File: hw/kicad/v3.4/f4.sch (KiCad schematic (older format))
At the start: 44 parts

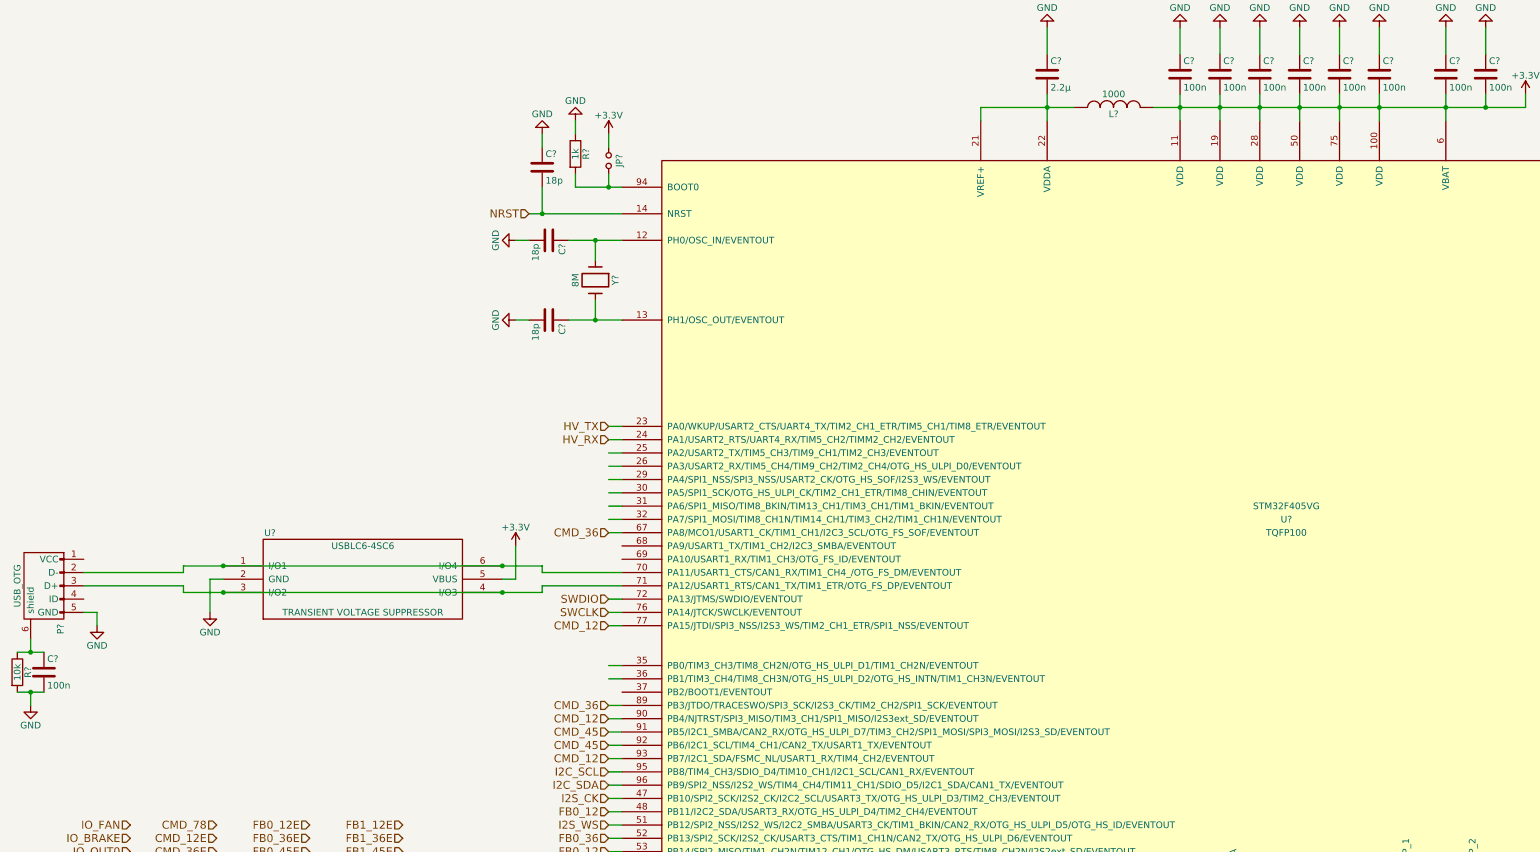
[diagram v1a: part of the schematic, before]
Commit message: f4 usb fix
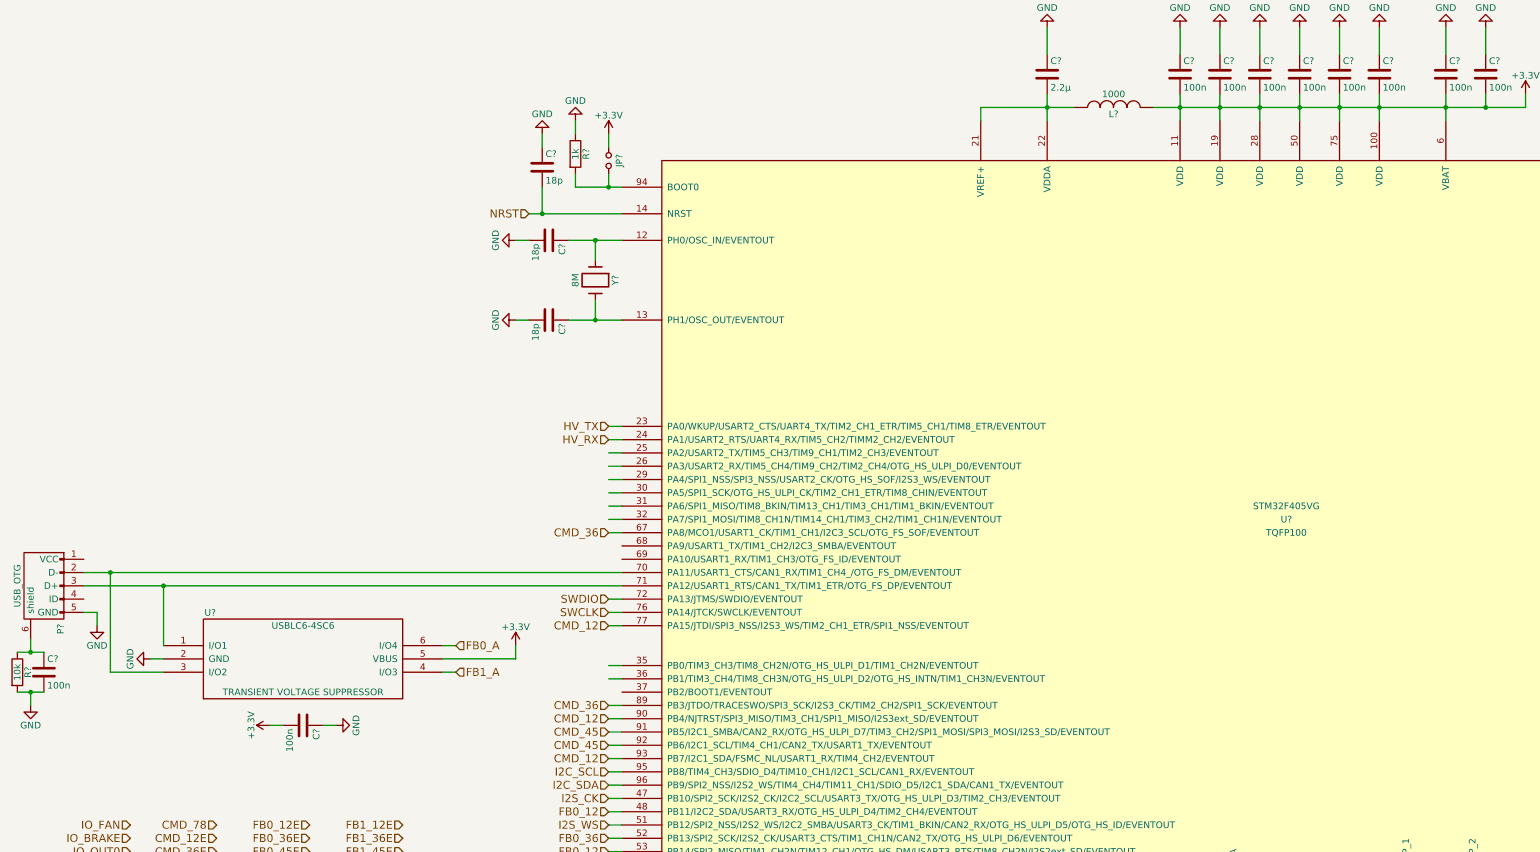
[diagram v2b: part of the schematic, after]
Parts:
- added C?: 100n, symbol C
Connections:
- wire segments 161 -> 159
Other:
- moved on the sheet: U?
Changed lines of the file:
@@
 	4800 3400 5200 3400
 Wire Wire Line
-	5200 4000 4800 4000
+	4800 4000 5200 4000
 Wire Wire Line
 	5000 3850 5000 4000
@@
 	9800 8500 9800 8600
 Wire Wire Line
-	11400 2500 11400 2300
-Wire Wire Line
-	10900 2500 10900 2300
-Wire Wire Line
-	10600 2500 10600 2300
-Wire Wire Line
-	10300 2500 10300 2300
-Wire Wire Line
-	10000 2500 10000 2300
-Wire Wire Line
-	9700 2500 9700 2300
-Wire Wire Line
-	9400 2500 9400 2300
+	11400 2300 11400 2500
+Wire Wire Line
+	10900 2300 10900 2500
+Wire Wire Line
+	10600 2300 10600 2500
+Wire Wire Line
+	10300 2300 10300 2500
+Wire Wire Line
+	10000 2300 10000 2500
+Wire Wire Line
+	9700 2300 9700 2500
+Wire Wire Line
+	9400 2300 9400 2500
 Wire Wire Line
 	9200 2400 12000 2400
@@
 	9400 2000 9400 1800
 Wire Wire Line
-	8400 2500 8400 2300
+	8400 2300 8400 2500
 $Comp
 L GND #PWR?
@@
 Text HLabel 1500 8100 0    60   Input ~ 0
 IO_OUT1
-Wire Wire Line
-	1900 5850 4600 5850
-Wire Wire Line
-	4600 5850 4600 5900
-Wire Wire Line
-	4600 5900 5200 5900
-Wire Wire Line
-	5200 6000 4600 6000
-Wire Wire Line
-	4600 6000 4600 6050
-Wire Wire Line
-	4600 6050 1900 6050
-Wire Wire Line
-	1900 6050 1900 6000
-Wire Wire Line
-	1900 6000 1150 6000
-Wire Wire Line
-	1150 5900 1900 5900
-Wire Wire Line
-	1900 5900 1900 5850
 $Comp
 L GND #PWR?
 U 1 1 5667D307
-P 2100 6200
-F 0 "#PWR?" H 2100 5950 50  0001 C CNN
-F 1 "GND" H 2100 6050 50  0000 C CNN
-F 2 "" H 2100 6200 60  0000 C CNN
-F 3 "" H 2100 6200 60  0000 C CNN
-	1    2100 6200
-	1    0    0    -1
-$EndComp
-Wire Wire Line
-	2100 6200 2100 5950
-Wire Wire Line
-	2100 5950 2200 5950
+P 1650 6550
+F 0 "#PWR?" H 1650 6300 50  0001 C CNN
+F 1 "GND" H 1650 6400 50  0000 C CNN
+F 2 "" H 1650 6550 60  0000 C CNN
+F 3 "" H 1650 6550 60  0000 C CNN
+	1    1650 6550
+	0    1    1    0
+$EndComp
 $Comp
 L +3.3V #PWR?
 U 1 1 5667D40D
-P 4400 5700
-F 0 "#PWR?" H 4400 5550 50  0001 C CNN
-F 1 "+3.3V" H 4400 5840 50  0000 C CNN
-F 2 "" H 4400 5700 60  0000 C CNN
-F 3 "" H 4400 5700 60  0000 C CNN
-	1    4400 5700
-	1    0    0    -1
-$EndComp
-Wire Wire Line
-	4400 5700 4400 5950
-Wire Wire Line
-	4400 5950 4300 5950
+P 4400 6450
+F 0 "#PWR?" H 4400 6300 50  0001 C CNN
+F 1 "+3.3V" H 4400 6590 50  0000 C CNN
+F 2 "" H 4400 6450 60  0000 C CNN
+F 3 "" H 4400 6450 60  0000 C CNN
+	1    4400 6450
+	1    0    0    -1
+$EndComp
 $Comp
 L USBLC6-4SC6 U?
 U 1 1 5667D8FF
-P 3250 5950
-F 0 "U?" H 2551 6298 50  0000 C CNN
-F 1 "USBLC6-4SC6" H 3250 6200 50  0000 C CNN
-F 2 "" H 3250 5950 60  0000 C CNN
-F 3 "" H 3250 5950 60  0000 C CNN
-F 4 "TRANSIENT VOLTAGE SUPPRESSOR" H 3250 5700 50  0000 C CNN "Description"
-	1    3250 5950
-	1    0    0    -1
-$EndComp
-Connection ~ 4300 6050
-Connection ~ 2200 6050
-Connection ~ 4300 5850
-Connection ~ 2200 5850
+P 2800 6550
+F 0 "U?" H 2101 6898 50  0000 C CNN
+F 1 "USBLC6-4SC6" H 2800 6800 50  0000 C CNN
+F 2 "" H 2800 6550 60  0000 C CNN
+F 3 "" H 2800 6550 60  0000 C CNN
+F 4 "TRANSIENT VOLTAGE SUPPRESSOR" H 2800 6300 50  0000 C CNN "Description"
+	1    2800 6550
+	1    0    0    -1
+$EndComp
 $Comp
 L USBLC6-4SC6 U?
@@
 Wire Wire Line
 	5100 2600 5100 2700
+Wire Wire Line
+	1150 6000 5200 6000
+Wire Wire Line
+	1150 5900 5200 5900
+Wire Wire Line
+	1750 6450 1750 6000
+Connection ~ 1750 6000
+Wire Wire Line
+	1750 6650 1350 6650
+Wire Wire Line
+	1350 6650 1350 5900
+Connection ~ 1350 5900
+Wire Wire Line
+	1650 6550 1750 6550
+Wire Wire Line
+	3850 6550 4400 6550
+Text HLabel 3950 6450 2    60   Input ~ 0
+FB0_A
+Text HLabel 3950 6650 2    60   Input ~ 0
+FB1_A
+Wire Wire Line
+	3850 6650 3950 6650
+Wire Wire Line
+	3850 6450 3950 6450
+$Comp
+L GND #PWR?
+U 1 1 56667EDB
+P 3050 7050
+F 0 "#PWR?" H 3050 6800 50  0001 C CNN
+F 1 "GND" H 3050 6900 50  0000 C CNN
+F 2 "" H 3050 7050 60  0000 C CNN
+F 3 "" H 3050 7050 60  0000 C CNN
+	1    3050 7050
+	0    -1   1    0
+$EndComp
+$Comp
+L +3.3V #PWR?
+U 1 1 566680A9
+P 2550 7050
+F 0 "#PWR?" H 2550 6900 50  0001 C CNN
+F 1 "+3.3V" H 2550 7190 50  0000 C CNN
+F 2 "" H 2550 7050 60  0000 C CNN
+F 3 "" H 2550 7050 60  0000 C CNN
+	1    2550 7050
+	0    -1   1    0
+$EndComp
+Wire Wire Line
+	3050 7050 2950 7050
+Wire Wire Line
+	2650 7050 2550 7050
+$Comp
+L C C?
+U 1 1 5666869C
+P 2800 7050
+F 0 "C?" H 2825 7150 50  0000 L CNN
+F 1 "100n" H 2825 6950 50  0000 L CNN
+F 2 "" H 2838 6900 30  0000 C CNN
+F 3 "" H 2800 7050 60  0000 C CNN
+	1    2800 7050
+	0    1    1    0
+$EndComp
+Wire Wire Line
+	4400 6550 4400 6450
 $EndSCHEMATC

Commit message: fb fix, cleanup
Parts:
- removed U? (x2): USBLC6-4SC6, symbol USBLC6-4SC6
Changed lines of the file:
@@
-	1    0    0    -1
-$EndComp
-$Comp
-L USBLC6-4SC6 U?
-U 1 1 5667DBA8
-P 5950 10500
-F 0 "U?" H 5251 10848 50  0000 C CNN
-F 1 "USBLC6-4SC6" H 5950 10750 50  0000 C CNN
-F 2 "" H 5950 10500 60  0000 C CNN
-F 3 "" H 5950 10500 60  0000 C CNN
-F 4 "TRANSIENT VOLTAGE SUPPRESSOR" H 5950 10250 50  0000 C CNN "Description"
-	1    5950 10500
-	1    0    0    -1
-$EndComp
-$Comp
-L USBLC6-4SC6 U?
-U 1 1 5667DC15
-P 8450 10500
-F 0 "U?" H 7751 10848 50  0000 C CNN
-F 1 "USBLC6-4SC6" H 8450 10750 50  0000 C CNN
-F 2 "" H 8450 10500 60  0000 C CNN
-F 3 "" H 8450 10500 60  0000 C CNN
-F 4 "TRANSIENT VOLTAGE SUPPRESSOR" H 8450 10250 50  0000 C CNN "Description"
-	1    8450 10500
 	1    0    0    -1
 $EndComp

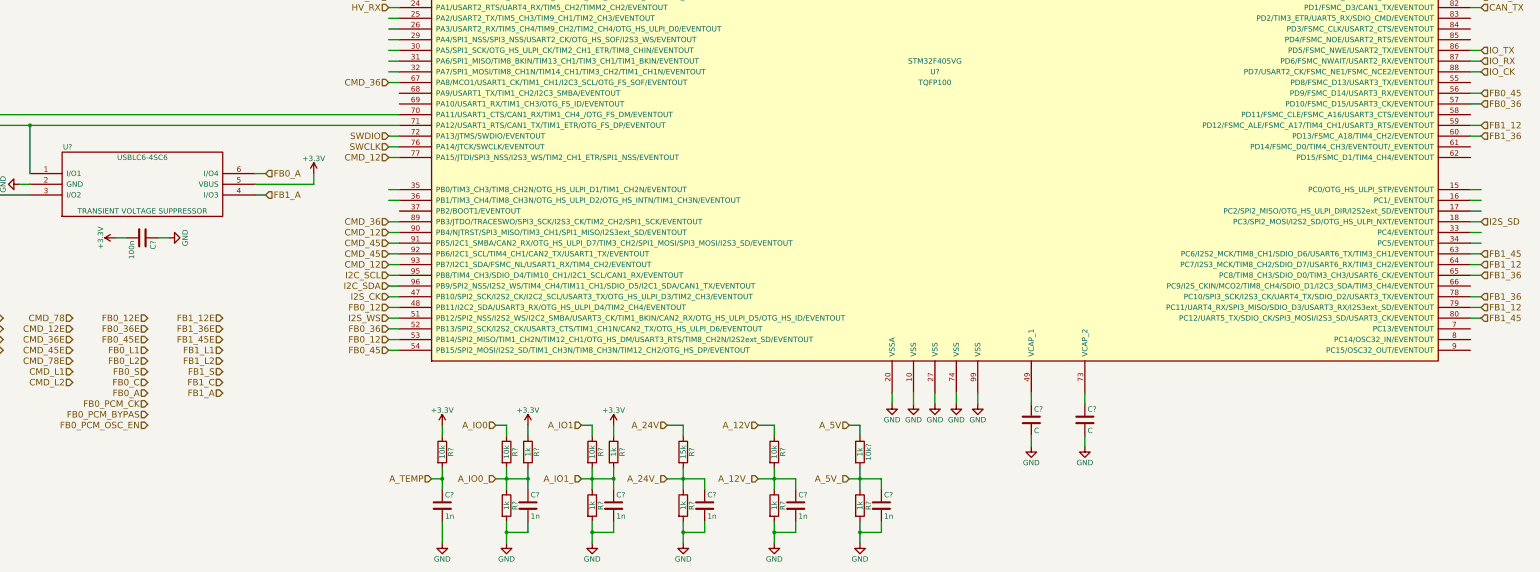
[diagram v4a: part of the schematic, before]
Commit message: +cur sense, f4 pin remap
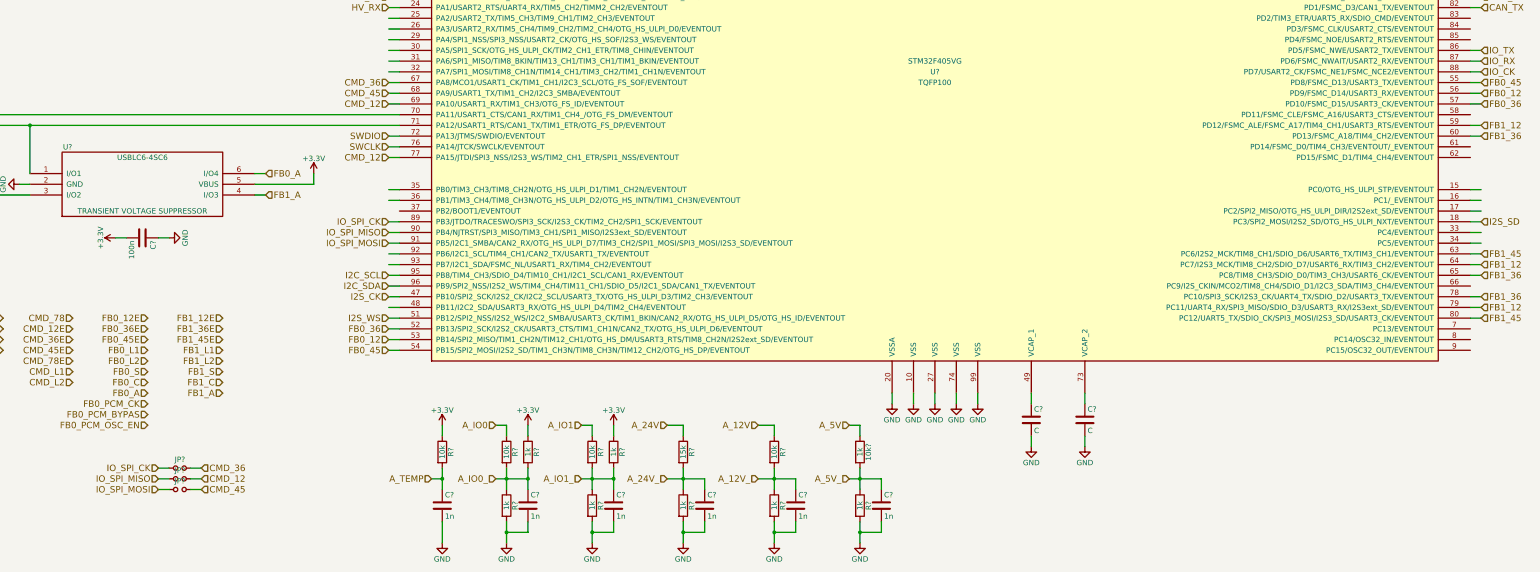
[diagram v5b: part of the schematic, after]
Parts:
- added JP? (x3): Jumper_NO_Small, symbol Jumper_NO_Small
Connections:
- net labels added: IO_SPI_CK, IO_SPI_MISO, IO_SPI_MOSI
- wire segments 159 -> 168
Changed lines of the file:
@@
 $Descr A3 16535 11693
 encoding utf-8
-Sheet 13 15
+Sheet 14 15
 Title ""
 Date ""
@@
 CMD_12
 Text HLabel 5100 7000 0    60   Input ~ 0
-CMD_12
-Text HLabel 5100 7300 0    60   Input ~ 0
+IO_SPI_MISO
+Text HLabel 5100 5800 0    60   Input ~ 0
 CMD_12
 Text HLabel 5100 5600 0    60   Input ~ 0
 CMD_36
 Text HLabel 5100 6900 0    60   Input ~ 0
-CMD_36
+IO_SPI_CK
 Text HLabel 5100 7100 0    60   Input ~ 0
-CMD_45
-Text HLabel 5100 7200 0    60   Input ~ 0
+IO_SPI_MOSI
+Text HLabel 5100 5700 0    60   Input ~ 0
 CMD_45
 Text HLabel 5100 8000 0    60   Input ~ 0
 FB0_12
-Text HLabel 5100 7700 0    60   Input ~ 0
+Text HLabel 15300 5700 2    60   Input ~ 0
 FB0_12
 Text HLabel 15300 3900 2    60   Input ~ 0
@@
 Text HLabel 15300 4100 2    60   Input ~ 0
 FB0_36
-Text HLabel 15300 5700 2    60   Input ~ 0
+Text HLabel 15300 5600 2    60   Input ~ 0
 FB0_45
 Text HLabel 5100 8100 0    60   Input ~ 0
@@
 Wire Wire Line
 	4400 6550 4400 6450
+Wire Wire Line
+	15300 5600 15200 5600
+Wire Wire Line
+	5100 5700 5200 5700
+Wire Wire Line
+	5100 5800 5200 5800
+$Comp
+L Jumper_NO_Small JP?
+U 1 1 5669DF96
+P 3150 9200
+F 0 "JP?" H 3150 9280 50  0000 C CNN
+F 1 "Jumper_NO_Small" H 3160 9140 50  0001 C CNN
+F 2 "" H 3150 9200 60  0000 C CNN
+F 3 "" H 3150 9200 60  0000 C CNN
+	1    3150 9200
+	1    0    0    -1
+$EndComp
+$Comp
+L Jumper_NO_Small JP?
+U 1 1 5669E03D
+P 3150 9300
+F 0 "JP?" H 3150 9380 50  0000 C CNN
+F 1 "Jumper_NO_Small" H 3160 9240 50  0001 C CNN
+F 2 "" H 3150 9300 60  0000 C CNN
+F 3 "" H 3150 9300 60  0000 C CNN
+	1    3150 9300
+	1    0    0    -1
+$EndComp
+$Comp
+L Jumper_NO_Small JP?
+U 1 1 5669E0D4
+P 3150 9400
+F 0 "JP?" H 3150 9480 50  0000 C CNN
+F 1 "Jumper_NO_Small" H 3160 9340 50  0001 C CNN
+F 2 "" H 3150 9400 60  0000 C CNN
+F 3 "" H 3150 9400 60  0000 C CNN
+	1    3150 9400
+	1    0    0    -1
+$EndComp
+Text HLabel 2950 9200 0    60   Input ~ 0
+IO_SPI_CK
+Text HLabel 2950 9300 0    60   Input ~ 0
+IO_SPI_MISO
+Text HLabel 2950 9400 0    60   Input ~ 0
+IO_SPI_MOSI
+Text HLabel 3350 9200 2    60   Input ~ 0
+CMD_36
+Text HLabel 3350 9400 2    60   Input ~ 0
+CMD_45
+Text HLabel 3350 9300 2    60   Input ~ 0
+CMD_12
+Wire Wire Line
+	2950 9200 3050 9200
+Wire Wire Line
+	2950 9300 3050 9300
+Wire Wire Line
+	2950 9400 3050 9400
+Wire Wire Line
+	3250 9200 3350 9200
+Wire Wire Line
+	3250 9300 3350 9300
+Wire Wire Line
+	3250 9400 3350 9400
 $EndSCHEMATC

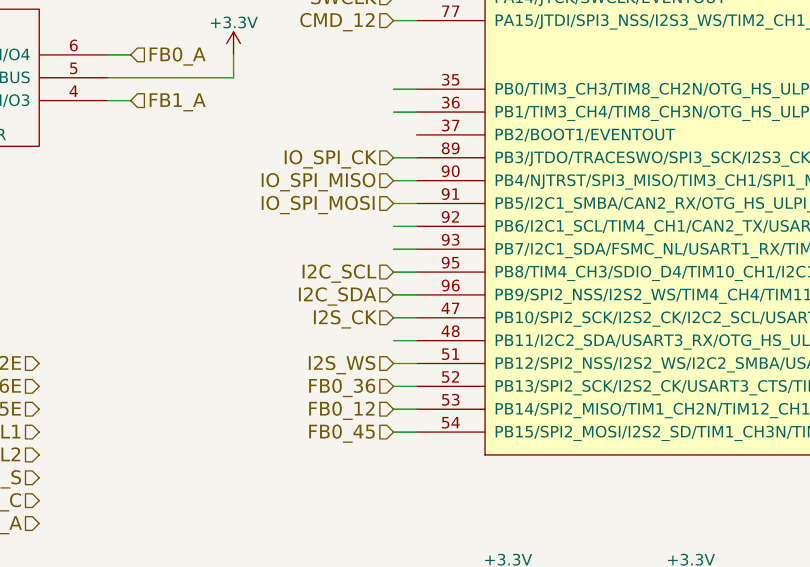
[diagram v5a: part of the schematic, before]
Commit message: io +spi
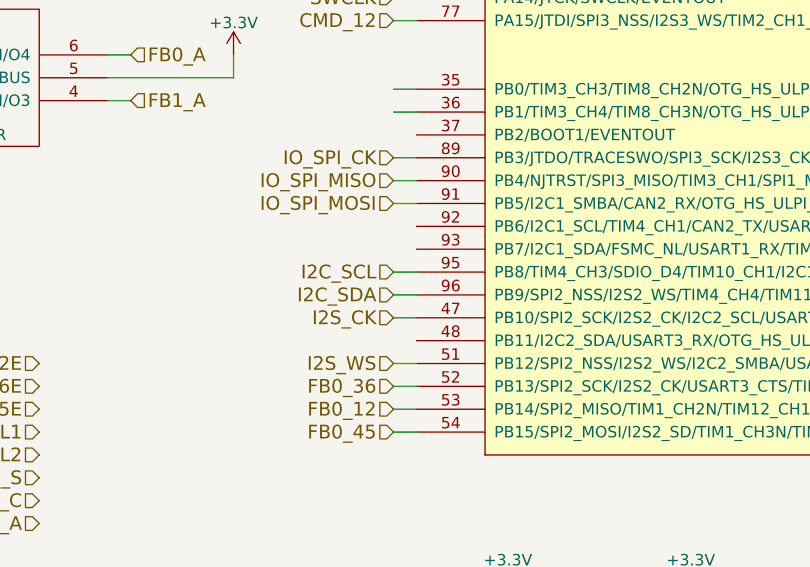
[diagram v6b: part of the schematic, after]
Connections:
- wire segments 168 -> 165
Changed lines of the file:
@@
 	5100 7000 5200 7000
-Wire Wire Line
-	5100 7300 5200 7300
 Wire Wire Line
 	15200 3900 15300 3900
@@
 	5100 7800 5200 7800
 Wire Wire Line
-	5100 7700 5200 7700
-Wire Wire Line
 	5100 7600 5200 7600
 Wire Wire Line
@@
 	5100 7400 5200 7400
 Wire Wire Line
-	5100 7200 5200 7200
-Wire Wire Line
 	5100 7100 5200 7100
